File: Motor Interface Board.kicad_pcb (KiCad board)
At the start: 2 copper layers, 54.2 x 44.3 mm, 16 parts, among them J1 Conn_02x05_Odd_Even, J2 Conn_02x05_Odd_Even, J3 Conn_01x02_Pin, J4 Conn_01x02_Pin, J5 Conn_01x20, J6 Conn_01x20, J7 Conn_02x04_Odd_Even, U1 TXB0108PW

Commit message: Add mounting holes + reconfigure GPIO to use SPI capable pins
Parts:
- moved J7 6.04 mm to (192.5, 34.8)
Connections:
- J6 pad 14: Net-(J6-Pin_14) -> unconnected-(J6-Pin_14-Pad14)
- J6 pad 15: Net-(J6-Pin_15) -> unconnected-(J6-Pin_15-Pad15)
- J6 pad 19: unconnected-(J6-Pin_19-Pad19) -> Net-(J6-Pin_19)
- J6 pad 20: unconnected-(J6-Pin_20-Pad20) -> Net-(J6-Pin_20)
- J7 pad 1: Net-(J6-Pin_14) -> Net-(J6-Pin_16)
- J7 pad 3: Net-(J6-Pin_15) -> Net-(J6-Pin_17)
- J7 pad 5: Net-(J6-Pin_16) -> Net-(J6-Pin_19)
- J7 pad 7: Net-(J6-Pin_17) -> Net-(J6-Pin_20)
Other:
- board size 54.2 x 44.3 mm -> 62.1 x 44.3 mm

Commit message: Move J2 to right of pico
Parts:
- added G***: LOGO, LOGO, F.Cu at (148.8, 52.2)
- moved J2 27.4 mm to (208.9, 50.0), turned to 0 degrees
- moved G*** 5.10 mm to (191.3, 52.4)
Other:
- board size 62.1 x 44.3 mm -> 70.3 x 44.3 mm
- board text added: "GND|MF-|DR-|PU-|XCOM"
- board text added: "XCOM|PU-|DR-|MF-|GND"
- board text removed: "X|P|D|M|G"

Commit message: Rotate J2, replace edge cut mounting holes with vias to ground
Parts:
- moved J2 7.91 mm to (211.0, 57.6), turned to 180 degrees
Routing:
- net (no net): vias 0 -> 4
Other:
- outline, holes or cut-outs redrawn
- board text removed: "GND|MF-|DR-|PU-|XCOM"

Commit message: Power pours + routing
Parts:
- moved C1 2.55 mm to (165.6, 66.6), turned to 180 degrees
- moved C2 2.03 mm to (154.1, 69.7)
- moved J2 1.49 mm to (209.5, 57.7)
- moved R2 1.42 mm to (152.2, 36.6), turned to 0 degrees
- moved R3 0.96 mm to (152.0, 32.2)
- moved D1 0.85 mm to (156.6, 36.2)
- moved U1 0.60 mm to (159.0, 69.2)
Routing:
- net /MF-: track 0.00 -> 78.3 mm, vias 0 -> 1
- net /DR-: track 0.00 -> 71.4 mm, vias 0 -> 1
- net /PU-: track 0.00 -> 68.4 mm, vias 0 -> 1
- net /XCOM: track 0.00 -> 58.8 mm, vias 0 -> 1
- net +3V3_Pi: track 0.00 -> 13.3 mm, vias 0 -> 1
- net /MF-_3V3: track 0.00 -> 13.1 mm, vias 0 -> 1
- net /DR-_3V3: track 0.00 -> 10.6 mm, vias 0 -> 1
- net Net-(J6-Pin_20): track 0.00 -> 9.38 mm
- net Net-(J6-Pin_19): track 0.00 -> 9.33 mm
- net Net-(J6-Pin_17): track 0.00 -> 8.97 mm
- net Net-(J6-Pin_16): track 0.00 -> 8.97 mm
- net +5V_IN: track 0.00 -> 8.89 mm
- net /XCOM_3V3: track 0.00 -> 8.48 mm, vias 0 -> 1
- net Net-(J6-Pin_1): track 0.00 -> 6.99 mm, vias 0 -> 1
- net /PU-_3V3: track 0.00 -> 4.66 mm
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- added copper zone on F.Cu, net +3V3
- added copper zone on F.Cu, net +5V
- added copper zone on B.Cu, net GND
- added copper zone on F.Cu, net GND

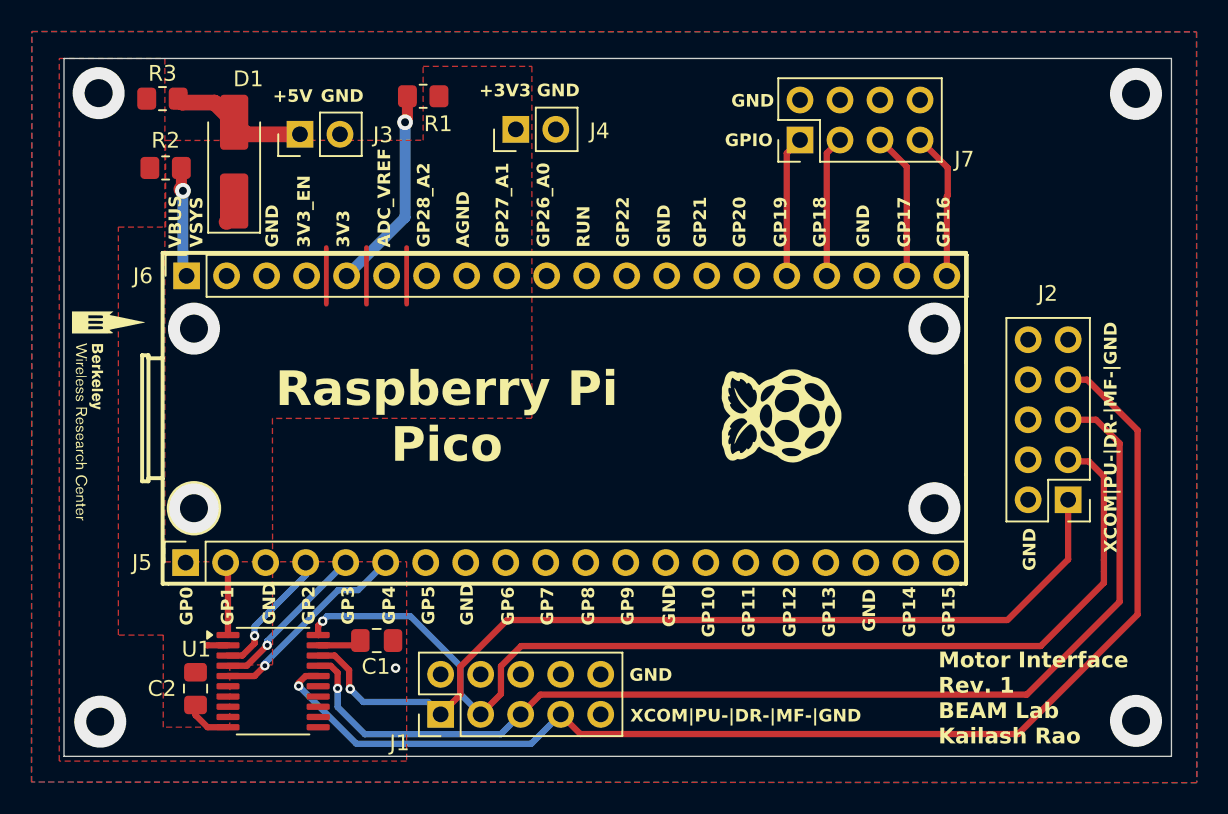
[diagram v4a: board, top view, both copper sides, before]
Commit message: GND stitching vias
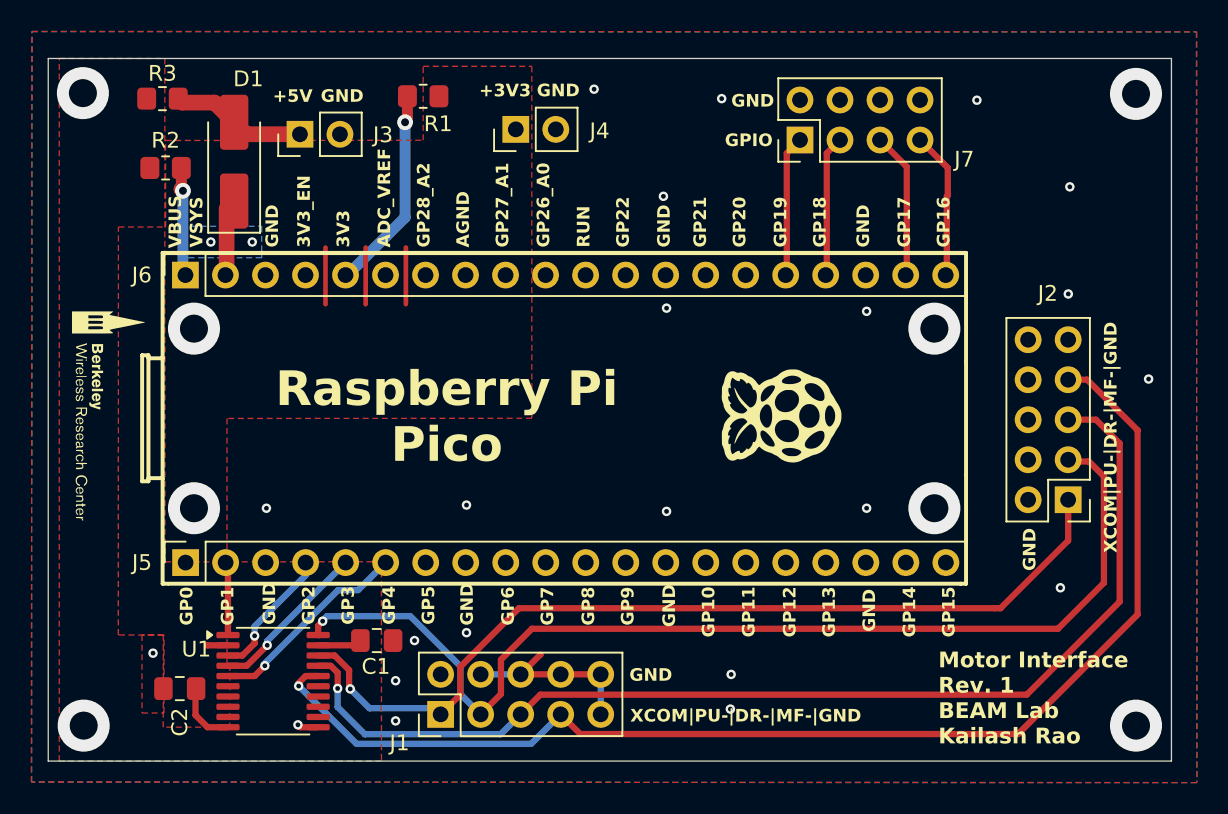
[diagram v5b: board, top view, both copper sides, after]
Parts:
- moved C2 1.00 mm to (153.1, 69.7), turned to 180 degrees
- moved J6 0.09 mm to (153.5, 43.4)
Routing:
- net GND: track 0.00 -> 13.3 mm, vias 9 -> 30
- net Net-(D1-K): track 0.68 -> 4.95 mm
- net +3V3: track 4.34 -> 5.39 mm, vias 0 -> 2
- net /XCOM: track 58.8 -> 58.2 mm
- added copper zone on B.Cu, net +3V3
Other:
- board size 70.3 x 44.3 mm -> 71.3 x 44.6 mm
